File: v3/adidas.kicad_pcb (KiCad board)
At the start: 2 copper layers, 152.7 x 107.2 mm, 36 parts, among them J1 ISP Header, J2 Shitty Add-on, J4 Battery, U1 MPU-6050, U2 ATTINY841-SSU

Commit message: refactor a bit
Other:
- board text added: ":: THE @DEAD10C5 LOVE YOU :: @iamgaraf yaya_pancho @craigmucka Hermit y3t1 @p0lr_ @thedevilsvoice"
- board text removed: ":: THE @DEAD10C5 LOVE YOU :: @p0lr_ Eddie the Yeti yaya_pancho @thedevilsvoice"
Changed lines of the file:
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@@
   (title_block
     (title "гопник badge")
-    (date "2023-04-03")
-    (rev "v0.2")
+    (date "2023-05-11")
+    (rev "v0.3")
     (company "DE:AD:10:C5")
     (comment 1 "Русский хардбасс")
@@
     (property "ki_keywords" "R res resistor")
     (attr smd)
-    (fp_text reference "R14" (at 0 1.82 180) (layer "B.SilkS") hide
+    (fp_text reference "R14" (at 0 1.82 -180) (layer "B.SilkS") hide
       (effects (font (size 1 1) (thickness 0.15)) (justify mirror))
     )
-    (fp_text value "470Ω" (at 0 -1.82 180) (layer "B.Fab") hide
+    (fp_text value "470Ω" (at 0 -1.82 -180) (layer "B.Fab") hide
       (effects (font (size 1 1) (thickness 0.15)) (justify mirror))
     )
@@
     (fp_line (start -1.6 -0.8) (end 1.6 -0.8)
       (stroke (width 0.1) (type solid)) (layer "B.Fab"))
-    (fp_text user "${REFERENCE}" (at 0 0 180) (layer "B.Fab") hide
+    (fp_text user "${REFERENCE}" (at 0 0 -180) (layer "B.Fab") hide
       (effects (font (size 0.8 0.8) (thickness 0.12)) (justify mirror))
     )
@@
     (fp_line (start -1.27 -3.81) (end -1.27 1.27)
       (stroke (width 0.1) (type solid)) (layer "B.Fab"))
-    (fp_text user "${REFERENCE}" (at 0 -1.27 90) (layer "B.Fab") hide
+    (fp_text user "${REFERENCE}" (at 0 -1.27 -270) (layer "B.Fab") hide
       (effects (font (size 1 1) (thickness 0.15)) (justify mirror))
     )
@@
     (fp_circle (center -5.225 0) (end -5.125 0)
       (stroke (width 0.2) (type solid)) (fill none) (layer "B.Fab"))
-    (fp_text user "Reset" (at -0.202 3.048 -90 unlocked) (layer "B.SilkS")
+    (fp_text user "Reset" (at -0.202 3.048 270 unlocked) (layer "B.SilkS")
       (effects (font (size 1 1) (thickness 0.15)) (justify mirror))
     )
@@
     (property "ki_keywords" "battery cell")
     (attr smd)
-    (fp_text reference "BT1" (at -9.15 -9.7 180) (layer "B.SilkS") hide
+    (fp_text reference "BT1" (at -9.15 -9.7 -180) (layer "B.SilkS") hide
       (effects (font (size 1 1) (thickness 0.15)) (justify mirror))
     )
-    (fp_text value "Battery Clip" (at 0 11 180) (layer "B.Fab") hide
+    (fp_text value "Battery Clip" (at 0 11 -180) (layer "B.Fab") hide
       (effects (font (size 1 1) (thickness 0.15)) (justify mirror))
     )
@@
     (fp_line (start -15.35 -2.55) (end -15.35 2.55)
       (stroke (width 0.1) (type solid)) (layer "B.Fab"))
-    (fp_text user "${REFERENCE}" (at -9.15 -9.7 180) (layer "B.Fab") hide
+    (fp_text user "${REFERENCE}" (at -9.15 -9.7 -180) (layer "B.Fab") hide
       (effects (font (size 1 1) (thickness 0.15)) (justify mirror))
     )
@@
     (effects (font (size 0.8 0.8) (thickness 0.15)) (justify mirror))
   )
-  (gr_text ":: THE @DEAD10C5 LOVE YOU ::\n@p0lr_\nEddie the Yeti\nyaya_pancho\n@thedevilsvoice " (at 231.6734 75.5904) (layer "B.SilkS")
+  (gr_text ":: THE @DEAD10C5 LOVE YOU ::\n@iamgaraf\nyaya_pancho\n@craigmucka\nHermit\ny3t1\n@p0lr_\n@thedevilsvoice" (at 231.6734 75.5904) (layer "B.SilkS")
     (effects (font (size 0.5 0.5) (thickness 0.075)) (justify mirror))
   )

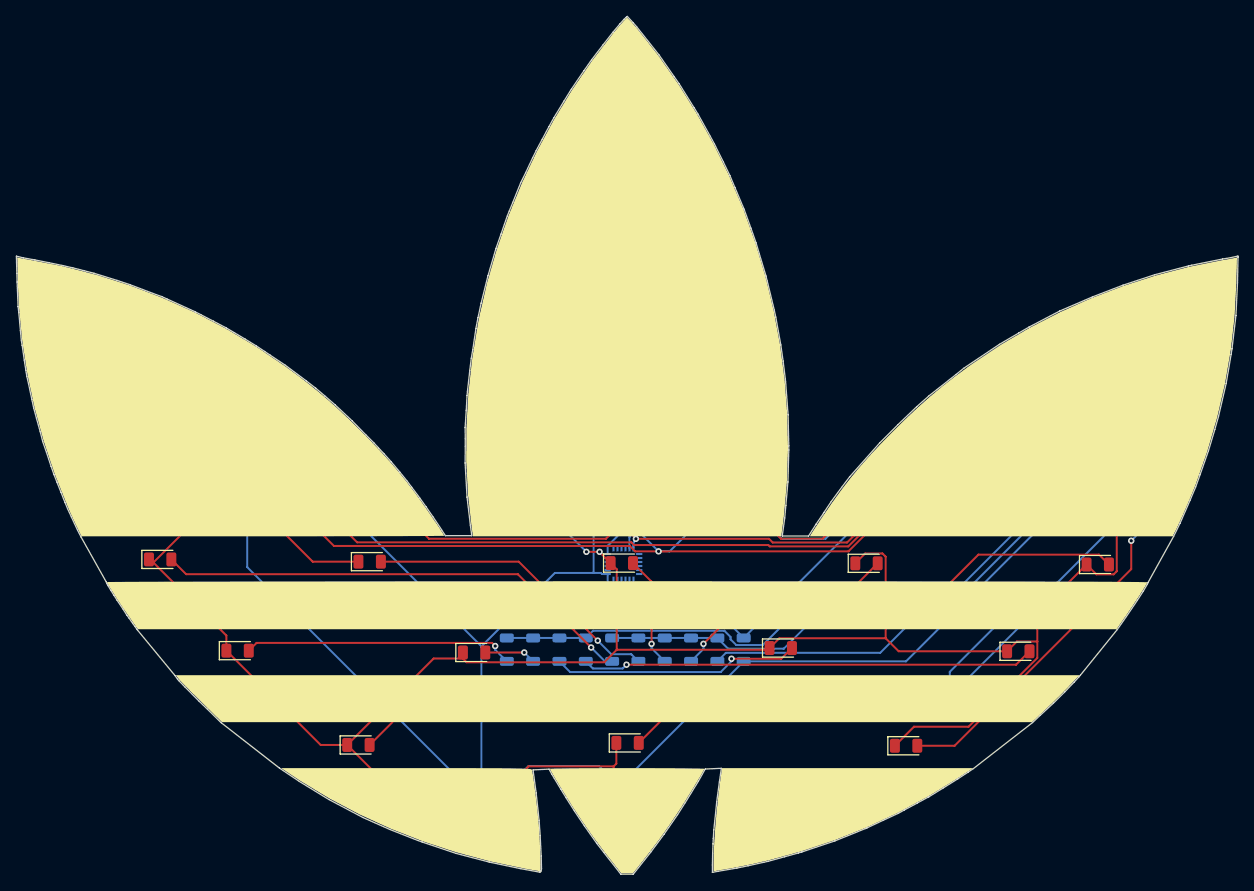
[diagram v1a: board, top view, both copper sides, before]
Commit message: more moounting holes
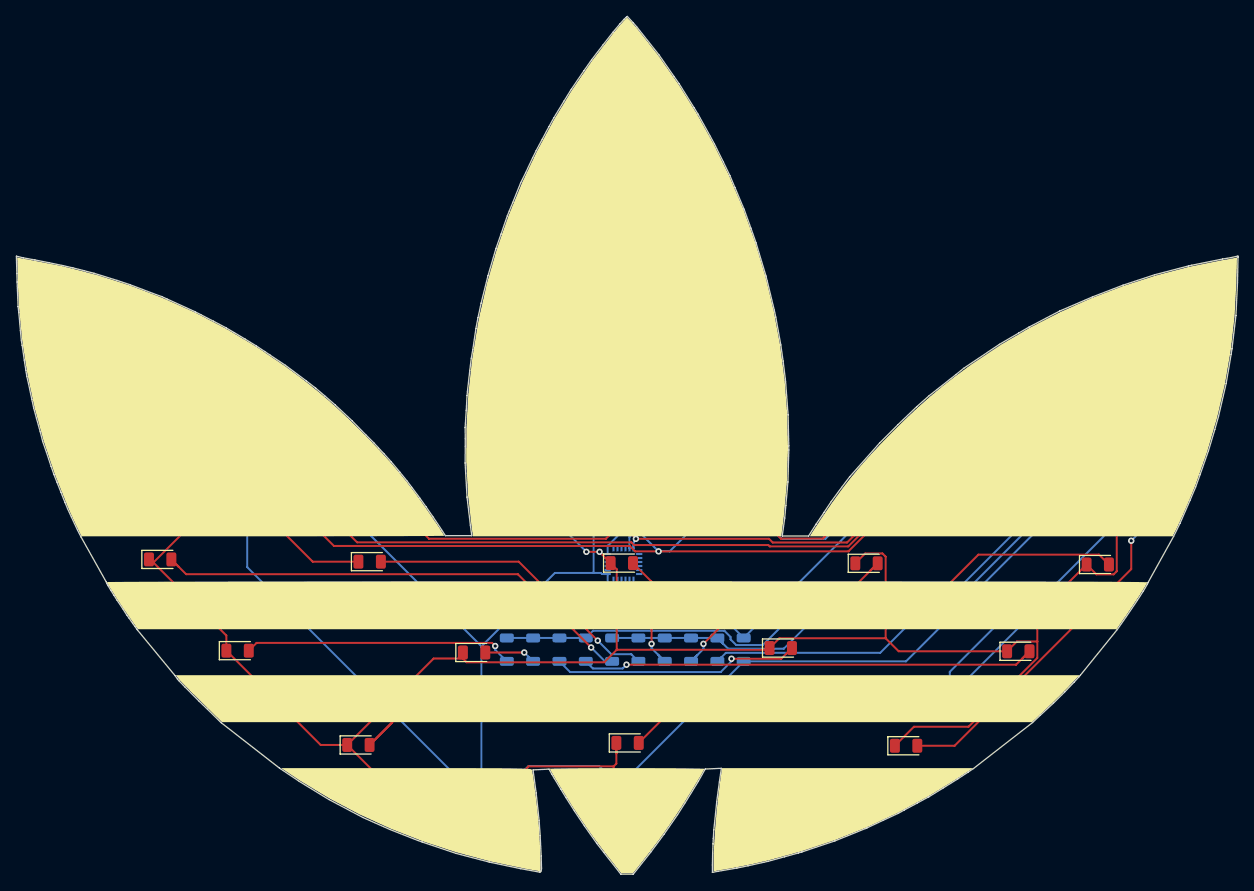
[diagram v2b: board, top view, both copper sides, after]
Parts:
- added hole-left: MountingHole_4.5mm, DEAD10C5:MountingHole_4.5mm, F.Cu at (234.6, 76.2)
- added hole-right: MountingHole_4.5mm, DEAD10C5:MountingHole_4.5mm, F.Cu at (96.6, 76.6)
- moved S2 2.14 mm to (234.6, 86.9)
- renumbered REF** to hole1
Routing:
- net Net-(D1-Pad2): track 71.2 -> 75.2 mm
- net VDD: track 196.4 -> 199.8 mm
- net Net-(D11-Pad2): track 28.8 -> 31.1 mm
- net GND: track 389.3 -> 391.3 mm
- net Net-(D8-Pad2): track 60.4 -> 61.7 mm
- net Net-(D7-Pad2): track 56.7 -> 57.9 mm
- net Net-(D10-Pad2): track 13.9 -> 15.1 mm
- net /13(SAO1): track 115.4 -> 116.6 mm
- net /5(LED Top Row): track 77.2 -> 78.2 mm
- net Net-(D6-Pad2): track 31.0 -> 32.0 mm
- net /9(SCK): track 173.2 -> 174.1 mm
- net Net-(D5-Pad2): track 6.44 -> 7.22 mm
- net Net-(D12-Pad2): track 55.0 -> 55.7 mm
- net /12(SAO2): track 92.4 -> 93.0 mm

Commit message: tune up reuse
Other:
- board text added: ":: THE @DEAD10C5 LOVE YOU :: justinjustin yaya_pancho @craigmucka Hermit y3t1 @p0lr_ @thedevilsvoice"
- board text removed: ":: THE @DEAD10C5 LOVE YOU :: @iamgaraf yaya_pancho @craigmucka Hermit y3t1 @p0lr_ @thedevilsvoice"
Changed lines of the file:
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@@
     (effects (font (size 1.5 1.5) (thickness 0.3) bold) (justify left bottom mirror))
   )
-  (gr_text ":: THE @DEAD10C5 LOVE YOU ::\n@iamgaraf\nyaya_pancho\n@craigmucka\nHermit\ny3t1\n@p0lr_\n@thedevilsvoice" (at 186.1566 135.763) (layer "B.SilkS")
+  (gr_text ":: THE @DEAD10C5 LOVE YOU ::\njustinjustin\nyaya_pancho\n@craigmucka\nHermit\ny3t1\n@p0lr_\n@thedevilsvoice" (at 186.1566 135.763) (layer "B.SilkS")
     (effects (font (size 0.5 0.5) (thickness 0.075)) (justify mirror))
   )

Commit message: update names
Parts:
- J4: value Battery -> батарея
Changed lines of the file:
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@@
     (property "ki_keywords" "R res resistor")
     (attr smd)
-    (fp_text reference "R14" (at 0 1.82 180) (layer "B.SilkS") hide
-      (effects (font (size 1 1) (thickness 0.15)) (justify mirror))
-    )
-    (fp_text value "470Ω" (at 0 -1.82 180) (layer "B.Fab") hide
+    (fp_text reference "R14" (at 0 1.82 -180) (layer "B.SilkS") hide
+      (effects (font (size 1 1) (thickness 0.15)) (justify mirror))
+    )
+    (fp_text value "470Ω" (at 0 -1.82 -180) (layer "B.Fab") hide
       (effects (font (size 1 1) (thickness 0.15)) (justify mirror))
     )
@@
     (fp_line (start -1.6 -0.8) (end 1.6 -0.8)
       (stroke (width 0.1) (type solid)) (layer "B.Fab"))
-    (fp_text user "${REFERENCE}" (at 0 0 180) (layer "B.Fab") hide
+    (fp_text user "${REFERENCE}" (at 0 0 -180) (layer "B.Fab") hide
       (effects (font (size 0.8 0.8) (thickness 0.12)) (justify mirror))
     )
@@
       (effects (font (size 1 1) (thickness 0.15)) (justify mirror))
     )
-    (fp_text value "Battery" (at 0 -5.31) (layer "B.SilkS")
+    (fp_text value "батарея" (at 0 -5.31) (layer "B.SilkS")
       (effects (font (size 1 1) (thickness 0.15)) (justify mirror))
     )
@@
     (fp_line (start -1.27 -3.81) (end -1.27 1.27)
       (stroke (width 0.1) (type solid)) (layer "B.Fab"))
-    (fp_text user "${REFERENCE}" (at 0 -1.27 90) (layer "B.Fab") hide
+    (fp_text user "${REFERENCE}" (at 0 -1.27 -270) (layer "B.Fab") hide
       (effects (font (size 1 1) (thickness 0.15)) (justify mirror))
     )
@@
     (fp_circle (center -5.225 0) (end -5.125 0)
       (stroke (width 0.2) (type solid)) (fill none) (layer "B.Fab"))
-    (fp_text user "Mode" (at 5.513 0.127 unlocked) (layer "B.SilkS")
+    (fp_text user "Mode" (at 5.513 0.127 unlocked) (layer "B.SilkS") hide
       (effects (font (size 1 1) (thickness 0.15)) (justify mirror))
     )
@@
     (fp_circle (center -5.225 0) (end -5.125 0)
       (stroke (width 0.2) (type solid)) (fill none) (layer "B.Fab"))
-    (fp_text user "Reset" (at -0.202 3.048 -90 unlocked) (layer "B.SilkS")
+    (fp_text user "Reset" (at -0.202 3.048 -90 unlocked) (layer "B.SilkS") hide
       (effects (font (size 1 1) (thickness 0.15)) (justify mirror))
     )
@@
     (property "ki_keywords" "battery cell")
     (attr smd)
-    (fp_text reference "BT1" (at -9.15 -9.7 180) (layer "B.SilkS") hide
-      (effects (font (size 1 1) (thickness 0.15)) (justify mirror))
-    )
-    (fp_text value "Battery Clip" (at 0 11 180) (layer "B.Fab") hide
+    (fp_text reference "BT1" (at -9.15 -9.7 -180) (layer "B.SilkS") hide
+      (effects (font (size 1 1) (thickness 0.15)) (justify mirror))
+    )
+    (fp_text value "Battery Clip" (at 0 11 -180) (layer "B.Fab") hide
       (effects (font (size 1 1) (thickness 0.15)) (justify mirror))
     )
@@
     (fp_line (start -15.35 -2.55) (end -15.35 2.55)
       (stroke (width 0.1) (type solid)) (layer "B.Fab"))
-    (fp_text user "${REFERENCE}" (at -9.15 -9.7 180) (layer "B.Fab") hide
-      (effects (font (size 1 1) (thickness 0.15)) (justify mirror))
-    )
+    (fp_text user "${REFERENCE}" (at -9.15 -9.7 -180) (layer "B.Fab") hide
+      (effects (font (size 1 1) (thickness 0.15)) (justify mirror))
+    )
